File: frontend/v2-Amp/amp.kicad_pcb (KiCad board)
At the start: 4 copper layers, 80 x 100 mm, 165 parts, among them K1 HK4100, K10 HK4100, K11 HK4100, K12 HK4100, K13 HK4100, K14 HK4100, K15 HK4100, K2 HK4100, K3 HK4100, K4 HK4100, K5 HK4100, K6 HK4100, K7 HK4100, K8 HK4100, K9 HK4100, P1 Antenna, P2 CONN_02X06, P3 TX Power Tap, P4 TX-IN, P5 RX IN, P6 12-13.8v, Q1 PZT2222A, Q2 RD16HHF1, T1 OUT_TRANSF, T2 BN-43-2402, U1 LP2951-50D

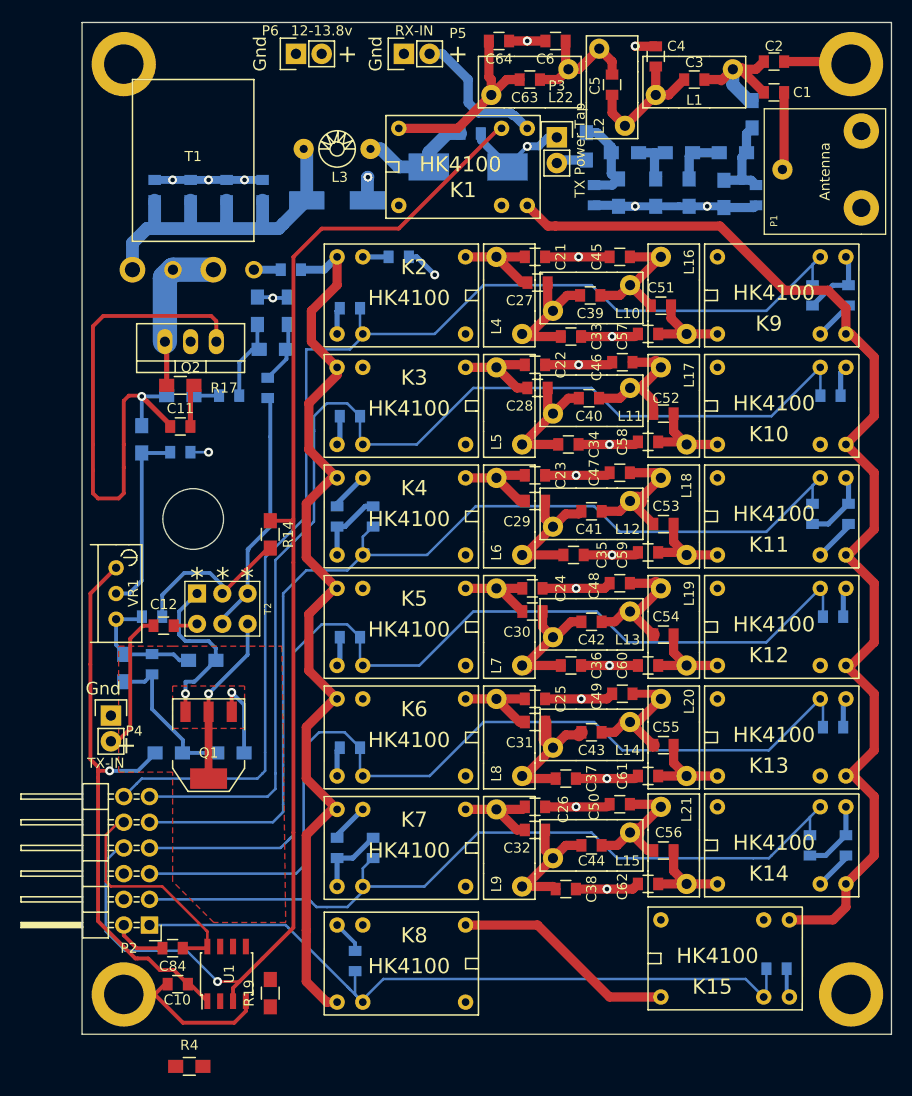
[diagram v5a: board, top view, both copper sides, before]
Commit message: Updates for v1.1 amp and V1.4 ADC
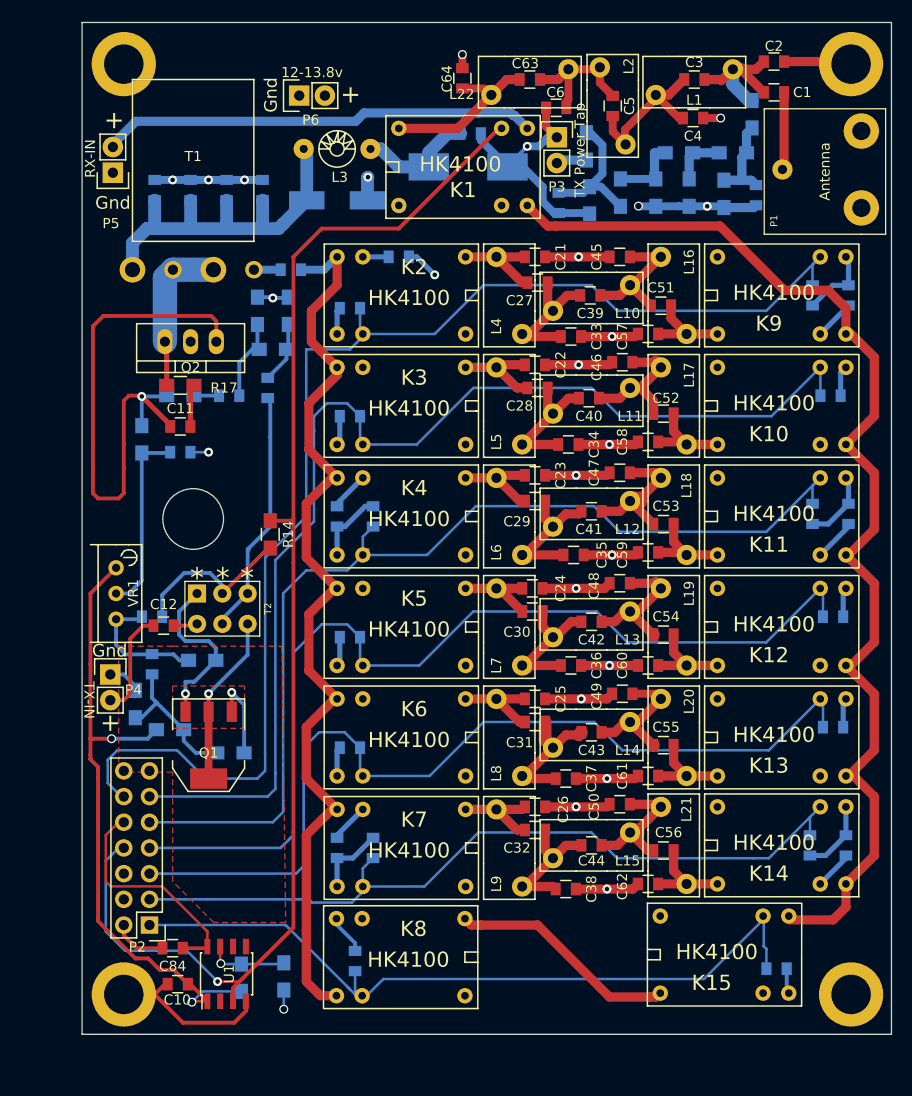
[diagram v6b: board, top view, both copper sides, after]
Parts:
- L13: value 455uH -> 455nH
- L7: value 642.5uH -> 642.5nH
- P2: value CONN_02X06 -> CONN_02X07; footprint Pin_Headers:Pin_Header_Angled_2x06 -> Pin_Headers:Pin_Header_Straight_2x07
- R19, R4: moved to B.Cu
- moved P5 31.1 mm to (118.0, 49.8), turned to 180 degrees
- moved R4 10.2 mm to (130.7, 129.4), turned to 270 degrees
- moved C4 7.12 mm to (175.4, 44.5), turned to 0 degrees
- moved C6 6.60 mm to (161.9, 43.4)
- moved C64 5.16 mm to (152.6, 40.5), turned to 90 degrees
- moved P6 4.14 mm to (136.5, 42.2)
- moved P4 4.06 mm to (117.8, 99.4)
- moved R26 3.96 mm to (168.2, 51.8), turned to 90 degrees
- moved R11 3.74 mm to (120.3, 102.4)
- moved C89 3.57 mm to (162.1, 52.8)
- moved R27 2.96 mm to (165.2, 52.6)
- moved R9 2.29 mm to (123.7, 104.9)
- moved R19 2.12 mm to (134.9, 129.3)
- moved C5 2.10 mm to (167.4, 43.2)
- moved L2 1.84 mm to (170.0, 48.3)
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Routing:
- net +12v: track 286.2 -> 380.7 mm
- net /Band6: track 163.9 -> 76.1 mm
- net Net-(K1-Pad1): track 14.4 -> 43.5 mm
- net GND: track 258.2 -> 266.6 mm, vias 24 -> 25
- net Net-(R19-Pad2): track 0.00 -> 8.01 mm, vias 0 -> 1
- net Net-(C10-Pad2): track 56.8 -> 64.5 mm, vias 1 -> 2
- net /Band0: track 121.2 -> 128.1 mm
- net Net-(C89-Pad1): track 9.29 -> 13.9 mm
- net Net-(C12-Pad1): track 14.2 -> 10.5 mm
- net Net-(C3-Pad1): track 14.2 -> 16.6 mm
- net Net-(C63-Pad1): track 19.4 -> 17.1 mm
- net Net-(R26-Pad2): track 6.01 -> 7.93 mm
- net Net-(C85-Pad1): track 16.0 -> 14.3 mm
- net Net-(C5-Pad1): track 13.1 -> 14.0 mm
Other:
- board text added: "Hermes Lite Pre-V2 PA 1.1 © 2016 W9JSW/ZL2APV"
- board text removed: "Hermes Lite Pre-V2 PA 1.0 © 2015 W9JSW/ZL2APV"

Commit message: Ver 1.1 changes
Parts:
- removed C12, C85, C87: 0.1uF, HERMESLITE:C_0805
- removed Q1: PZT2222A, TO_SOT_Packages_SMD:SOT-223
- removed R11: 1k, Resistors_SMD:R_0805_HandSoldering
- removed R13: 4.7, Resistors_SMD:R_0805_HandSoldering
- removed R18: 47, Resistors_SMD:R_0805_HandSoldering
- removed R9: 1.2k, Resistors_SMD:R_0805_HandSoldering
- removed T2: BN-43-2402, HERMESLITE:TRANSF
- added L23: 100nH, Resistors_SMD:R_0805_HandSoldering, B.Cu at (123.4, 63.0)
- C1, C11, R17: moved to B.Cu
- L1, L2, L22: footprint HERMESLITE:Choke_Toroid -> Resistors_SMD:R_0805_HandSoldering
- Q2: footprint Transistors_TO-220:TO-220_Neutral123_Vertical -> TO_SOT_Packages_THT:TO-220_Neutral123_Vertical
- R10: value 18 -> 0
- R12, R8: value 270 -> DNI
- moved C64 92.5 mm to (168.3, 131.7), turned to 180 degrees
- moved L1 92.2 mm to (158.6, 127.9), turned to 270 degrees
- moved C3 89.5 mm to (156.0, 128.0), turned to 90 degrees
- moved L22 89.5 mm to (166.9, 127.8), turned to 270 degrees
- moved C4 88.8 mm to (158.2, 131.6), turned to 180 degrees
- moved C2 87.9 mm to (159.6, 123.5)
- moved C63 87.5 mm to (169.4, 127.6), turned to 90 degrees
- moved C5 87.5 mm to (163.0, 130.6), turned to 180 degrees
- moved C6 80.5 mm to (168.0, 123.7), turned to 0 degrees
- moved L2 79.8 mm to (162.9, 127.8), turned to 0 degrees
- moved R14 37.5 mm to (130.7, 123.0), turned to 180 degrees
- moved VR1 18.7 mm to (126.2, 105.9), turned to 270 degrees
- moved R17 7.78 mm to (118.0, 66.9), turned to 270 degrees
- moved C11 6.57 mm to (121.0, 69.5), turned to 270 degrees
- moved R1 4.51 mm to (176.7, 43.9), turned to 180 degrees
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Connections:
- C2 pad 1: Net-(C1-Pad2) -> Net-(C2-Pad1)
- C3 pad 2: Net-(C1-Pad2) -> Net-(C2-Pad1)
- K1 pad 3: Net-(C63-Pad1) -> Net-(C1-Pad2)
- K15 pad 4: Net-(K15-Pad4) -> Net-(C63-Pad1)
- K8 pad 4: Net-(K15-Pad4) -> Net-(C2-Pad1)
- L1 pad 1: Net-(C1-Pad2) -> Net-(C2-Pad1)
- P4 pad 2: Net-(C12-Pad1) -> Net-(C86-Pad1)
- Q2 pad 1: Net-(C11-Pad2) -> Net-(L23-Pad2)
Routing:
- net GND: track 266.6 -> 185.0 mm, vias 25 -> 39
- net Net-(C11-Pad2): track 55.5 -> 24.6 mm, vias 1 -> 0
- net +12v: track 380.7 -> 351.9 mm
- net Net-(C1-Pad2): track 16.3 -> 41.6 mm
- net Net-(K15-Pad4): track 22.7 -> 0.00 mm
- net Net-(Q1-Pad3): track 17.1 -> 0.00 mm, vias 1 -> 0
- net Net-(Q1-Pad2): track 16.9 -> 0.00 mm, vias 1 -> 0
- net Net-(C10-Pad2): track 64.5 -> 47.9 mm, vias 2 -> 1
- net Net-(C9-Pad2): track 18.5 -> 34.4 mm, vias 0 -> 1
- net Net-(C85-Pad1): track 14.3 -> 0.00 mm
- net Net-(C86-Pad1): track 24.5 -> 38.5 mm
- net Net-(C2-Pad1): track 0.00 -> 12.7 mm
- net Net-(C12-Pad1): track 10.5 -> 0.00 mm
- net Net-(Q1-Pad1): track 8.38 -> 0.00 mm, vias 1 -> 0
- net Net-(C63-Pad1): track 17.1 -> 9.60 mm
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- removed copper zone on F.Cu, net Net-(Q1-Pad2)
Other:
- board text added: "Hermes Lite Pre-V2 PA 1.2 © 2016 W9JSW"
- board text removed: "*"
- board text removed: "Hermes Lite Pre-V2 PA 1.1 © 2016 W9JSW/ZL2APV"

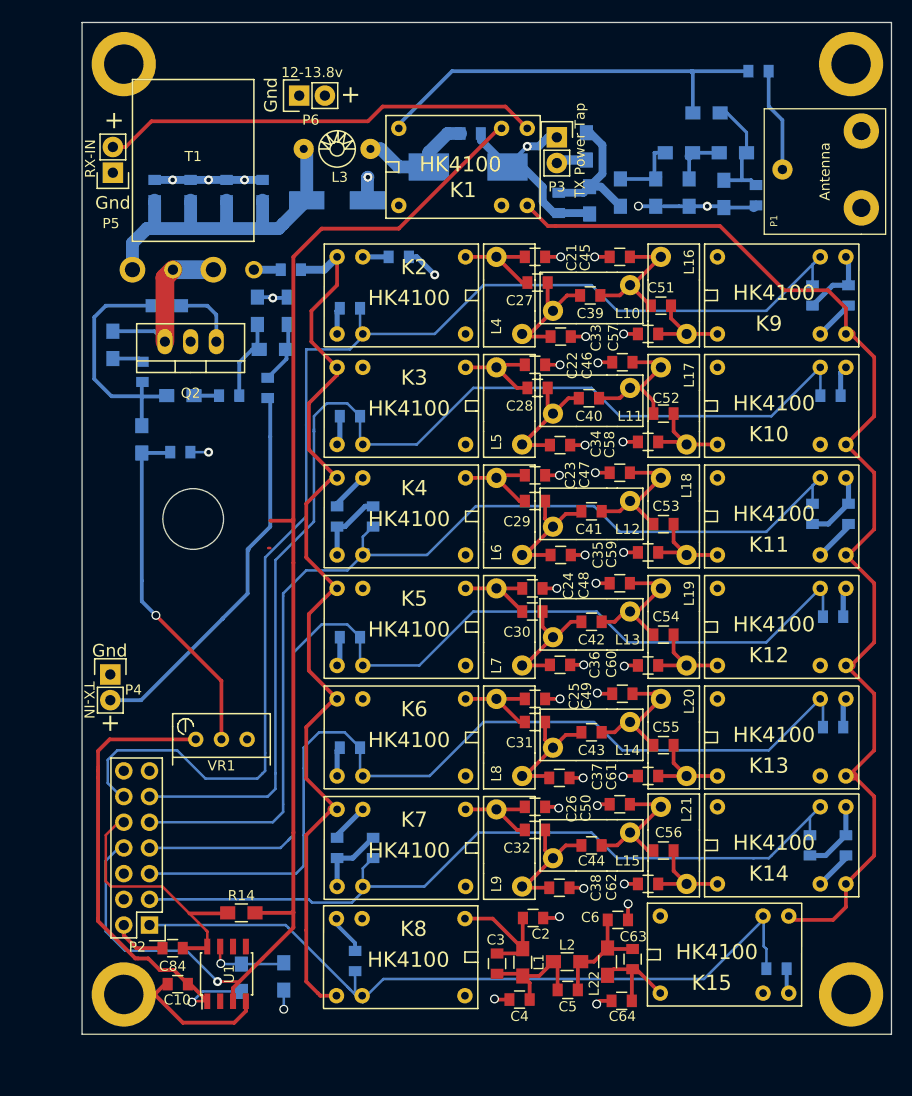
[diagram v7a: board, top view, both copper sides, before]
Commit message: Updates to 10M filter
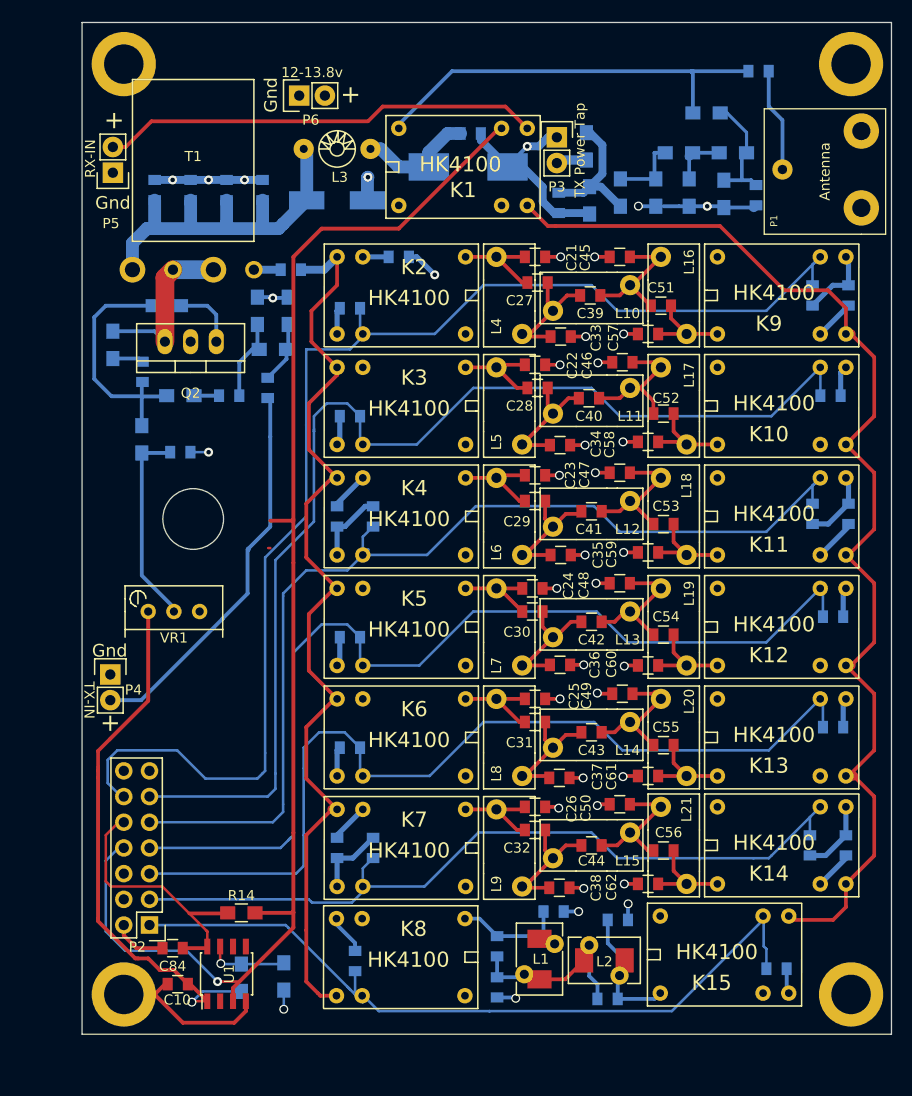
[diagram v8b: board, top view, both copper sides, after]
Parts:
- removed C63: DNI, HERMESLITE:C_0805
- removed C64: 82pF, HERMESLITE:C_0805
- removed L22: 363nH, Resistors_SMD:R_0805_HandSoldering
- C2: value 82pf -> 100pf; moved to B.Cu
- C3: moved to B.Cu
- C4: value 150pf -> 180pf; moved to B.Cu
- C5: value 56pf -> DNI; moved to B.Cu
- C6: value 150pf -> 100pf; moved to B.Cu
- L1: value 363nH -> 330nH; footprint Resistors_SMD:R_0805_HandSoldering -> HERMESLITE:inductor
- L2: value 243nH -> 330nH; footprint Resistors_SMD:R_0805_HandSoldering -> HERMESLITE:inductor
- moved VR1 13.5 mm to (121.5, 93.2)
- moved C5 4.04 mm to (166.9, 131.5)
- moved L2 3.69 mm to (166.6, 127.7)
- moved C4 2.53 mm to (156.0, 130.4), turned to 270 degrees
- moved C2 2.13 mm to (161.6, 122.9)
- moved C3 1.71 mm to (156.0, 126.3)
- moved L1 1.68 mm to (160.2, 127.6)
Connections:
- K15 pad 4: Net-(C63-Pad1) -> Net-(C5-Pad1)
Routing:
- net Net-(C9-Pad2): track 34.4 -> 19.8 mm, vias 1 -> 0
- net Net-(C63-Pad1): track 9.60 -> 0.00 mm
- net Net-(C3-Pad1): track 11.8 -> 19.1 mm
- net Net-(C10-Pad2): track 47.9 -> 53.6 mm
- net Net-(C5-Pad1): track 11.4 -> 14.5 mm
- net Net-(C2-Pad1): track 12.7 -> 15.3 mm
- net GND: track 185.0 -> 183.7 mm, vias 39 -> 38
- net /Band6: track 76.1 -> 77.3 mm
